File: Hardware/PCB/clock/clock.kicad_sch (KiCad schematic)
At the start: 62 parts, among them J1 AudioJack2, J2 Synth_power_2x5, J3 AudioJack2, J4 AudioJack2, J5 AudioJack2, J6 AudioJack2, J7 AudioJack2, J8 Conn_02x04_Odd_Even, J9 Conn_02x04_Odd_Even, SW1 RotaryEncoder, SW2 SW_Push, U1 40106

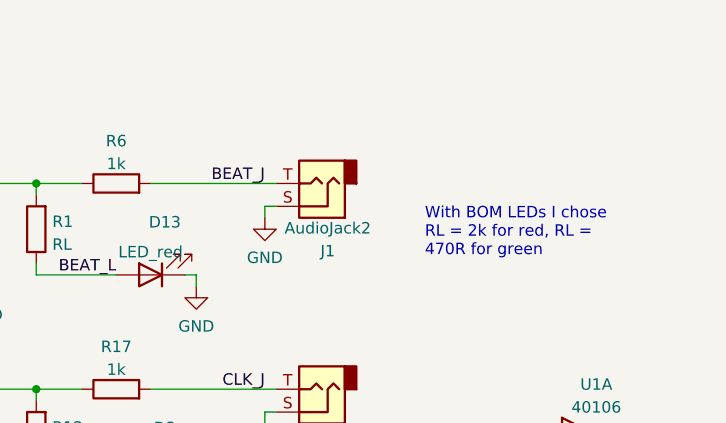
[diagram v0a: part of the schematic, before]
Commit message: LED notes on sch
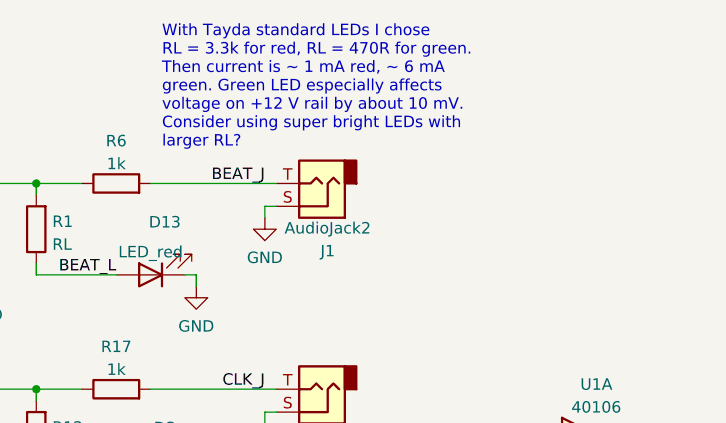
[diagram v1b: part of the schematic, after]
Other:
- note added: "With Tayda standard LEDs I chose RL = 3.3k for red, RL = 470R for green. Then current is ~ 1 mA red, ~ 6 mA green. Green LED especially affects voltage on +12 V rail by about 10 mV. Consider using super bright LEDs with larger RL?"
- note removed: "With BOM LEDs I chose RL = 2k for red, RL = 470R for green"
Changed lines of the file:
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@@
     )
   )
-  (text "With BOM LEDs I chose\nRL = 2k for red, RL = \n470R for green"
-    (at 233.68 40.005 0)
+  (text "With Tayda standard LEDs I chose\nRL = 3.3k for red, RL = 470R for green.\nThen current is ~ 1 mA red, ~ 6 mA\ngreen. Green LED especially affects\nvoltage on +12 V rail by about 10 mV.\nConsider using super bright LEDs with\nlarger RL?"
+    (at 204.47 27.94 0)
     (effects (font (size 1.27 1.27)) (justify left bottom))
   )

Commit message: PCB touch ups, panel
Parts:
- added GRAF3: AO logo, ao_tht:analogoutput_12mm, symbol ao_symbols:Graphic
- GRAF2: value Behind -> CC0 logo; footprint clock:clock_panel_holes -> ao_tht:CC0_logo
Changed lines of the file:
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@@
   (no_connect (at 260.35 77.47))
   (no_connect (at 157.48 60.96))
+  (polyline (pts (xy 13.97 13.97) (xy 13.97 160.02))
+    (stroke (width 0) (type default) (color 0 0 0 0))
+  )
   (wire (pts (xy 22.86 58.42) (xy 22.86 81.28))
     (stroke (width 0) (type default) (color 0 0 0 0))
@@
     (stroke (width 0) (type default) (color 0 0 0 0))
   )
+  (polyline (pts (xy 86.36 13.97) (xy 86.36 160.02))
+    (stroke (width 0) (type default) (color 0 0 0 0))
+  )
   (wire (pts (xy 139.7 78.74) (xy 142.24 78.74))
     (stroke (width 0) (type default) (color 0 0 0 0))
@@
     (stroke (width 0) (type default) (color 0 0 0 0))
   )
+  (polyline (pts (xy 13.97 13.97) (xy 86.36 13.97))
+    (stroke (width 0) (type default) (color 0 0 0 0))
+  )
   (wire (pts (xy 215.9 35.56) (xy 215.9 34.29))
     (stroke (width 0) (type default) (color 0 0 0 0))
@@
     (stroke (width 0) (type default) (color 0 0 0 0))
   )
+  (polyline (pts (xy 86.36 160.02) (xy 13.97 160.02))
+    (stroke (width 0) (type default) (color 0 0 0 0))
+  )
   (wire (pts (xy 24.13 104.14) (xy 17.78 104.14))
     (stroke (width 0) (type default) (color 0 0 0 0))
@@
     )
   )
-  (symbol (lib_id "ao_symbols:Graphic") (at 250.19 144.78 0) (unit 1)
-    (in_bom yes) (on_board yes)
-    (property "Reference" "GRAF2" (id 0) (at 257.2512 143.6116 0)
-      (effects (font (size 1.27 1.27)) (justify left))
-    )
-    (property "Value" "Behind" (id 1) (at 257.2512 145.923 0)
-      (effects (font (size 1.27 1.27)) (justify left))
-    )
-    (property "Footprint" "clock:clock_panel_holes" (id 2) (at 250.19 144.78 0)
-      (effects (font (size 1.27 1.27)) hide)
-    )
-    (property "Datasheet" "" (id 3) (at 250.19 144.78 0)
-      (effects (font (size 1.27 1.27)) hide)
-    )
-    (property "Config" "DNF" (id 4) (at 250.19 144.78 0)
-      (effects (font (size 1.27 1.27)) hide)
-    )
-  )
   (symbol (lib_id "ao_symbols:+5V_1") (at 50.8 96.52 0) (unit 1)
     (in_bom yes) (on_board yes) (fields_autoplaced)
@@
     (pin "2")
   )
+  (symbol (lib_id "ao_symbols:Graphic") (at 250.19 149.86 0) (unit 1)
+    (in_bom yes) (on_board yes)
+    (property "Reference" "GRAF3" (id 0) (at 257.2512 148.6916 0)
+      (effects (font (size 1.27 1.27)) (justify left))
+    )
+    (property "Value" "AO logo" (id 1) (at 257.2512 151.003 0)
+      (effects (font (size 1.27 1.27)) (justify left))
+    )
+    (property "Footprint" "ao_tht:analogoutput_12mm" (id 2) (at 250.19 149.86 0)
+      (effects (font (size 1.27 1.27)) hide)
+    )
+    (property "Datasheet" "" (id 3) (at 250.19 149.86 0)
+      (effects (font (size 1.27 1.27)) hide)
+    )
+    (property "Config" "DNF" (id 4) (at 250.19 149.86 0)
+      (effects (font (size 1.27 1.27)) hide)
+    )
+  )
   (symbol (lib_id "power:+5V") (at 144.145 22.86 0) (unit 1)
     (in_bom yes) (on_board yes) (fields_autoplaced)
@@
     (pin "2")
   )
+  (symbol (lib_id "ao_symbols:Graphic") (at 250.19 143.51 0) (unit 1)
+    (in_bom yes) (on_board yes)
+    (property "Reference" "GRAF2" (id 0) (at 257.2512 142.3416 0)
+      (effects (font (size 1.27 1.27)) (justify left))
+    )
+    (property "Value" "CC0 logo" (id 1) (at 257.2512 144.653 0)
+      (effects (font (size 1.27 1.27)) (justify left))
+    )
+    (property "Footprint" "ao_tht:CC0_logo" (id 2) (at 250.19 143.51 0)
+      (effects (font (size 1.27 1.27)) hide)
+    )
+    (property "Datasheet" "" (id 3) (at 250.19 143.51 0)
+      (effects (font (size 1.27 1.27)) hide)
+    )
+    (property "Config" "DNF" (id 4) (at 250.19 143.51 0)
+      (effects (font (size 1.27 1.27)) hide)
+    )
+  )
   (symbol (lib_id "ao_symbols:TestPoint") (at 104.14 199.39 0) (unit 1)
     (in_bom yes) (on_board yes) (fields_autoplaced)
@@
       (reference "GRAF1") (unit 1) (value "Holes") (footprint "clock:clock_panel_holes")
     )
-    (path "/3148a9e6-1e75-4e2a-b943-102cc5541cb8"
-      (reference "GRAF2") (unit 1) (value "Behind") (footprint "clock:clock_panel_holes")
+    (path "/dde30d9f-a4ed-4a0d-91aa-0eba4eadd958"
+      (reference "GRAF2") (unit 1) (value "CC0 logo") (footprint "ao_tht:CC0_logo")
+    )
+    (path "/419f3ecf-7b71-4a84-b495-f34f5fc91026"
+      (reference "GRAF3") (unit 1) (value "AO logo") (footprint "ao_tht:analogoutput_12mm")
     )
     (path "/9aa227a4-5918-4955-a2f5-b1e4c4fe38eb"

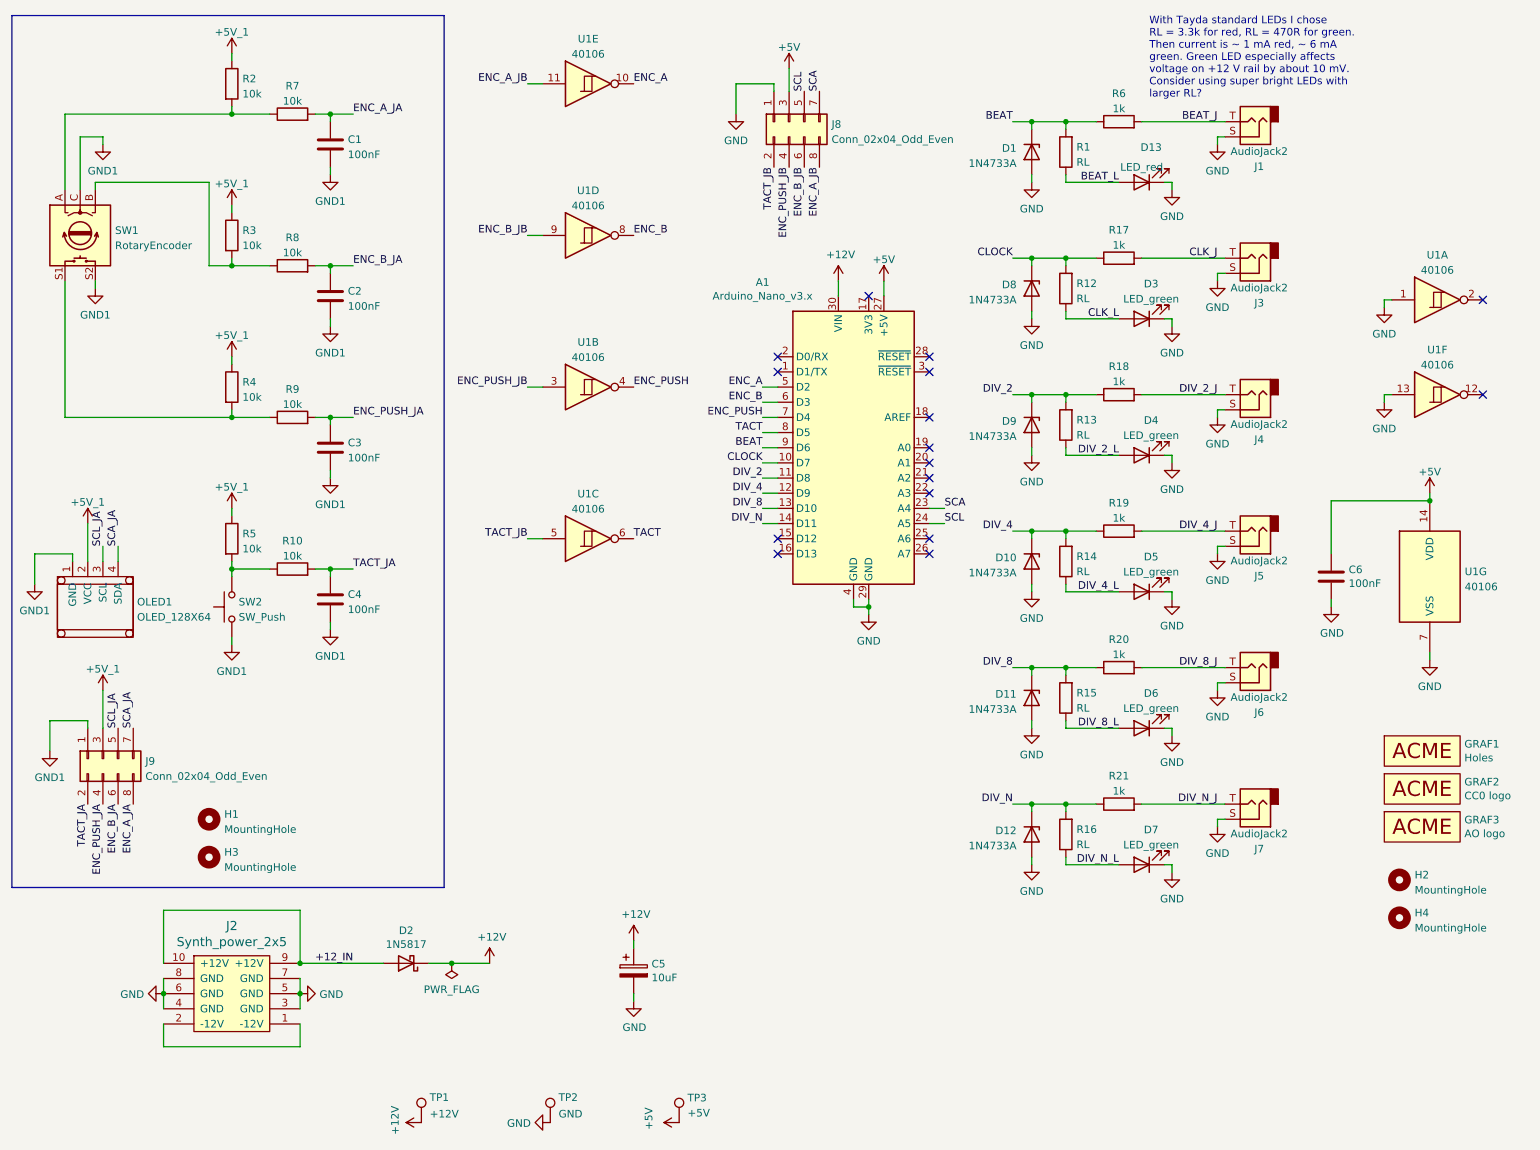
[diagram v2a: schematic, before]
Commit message: typo; OLED panel footprint
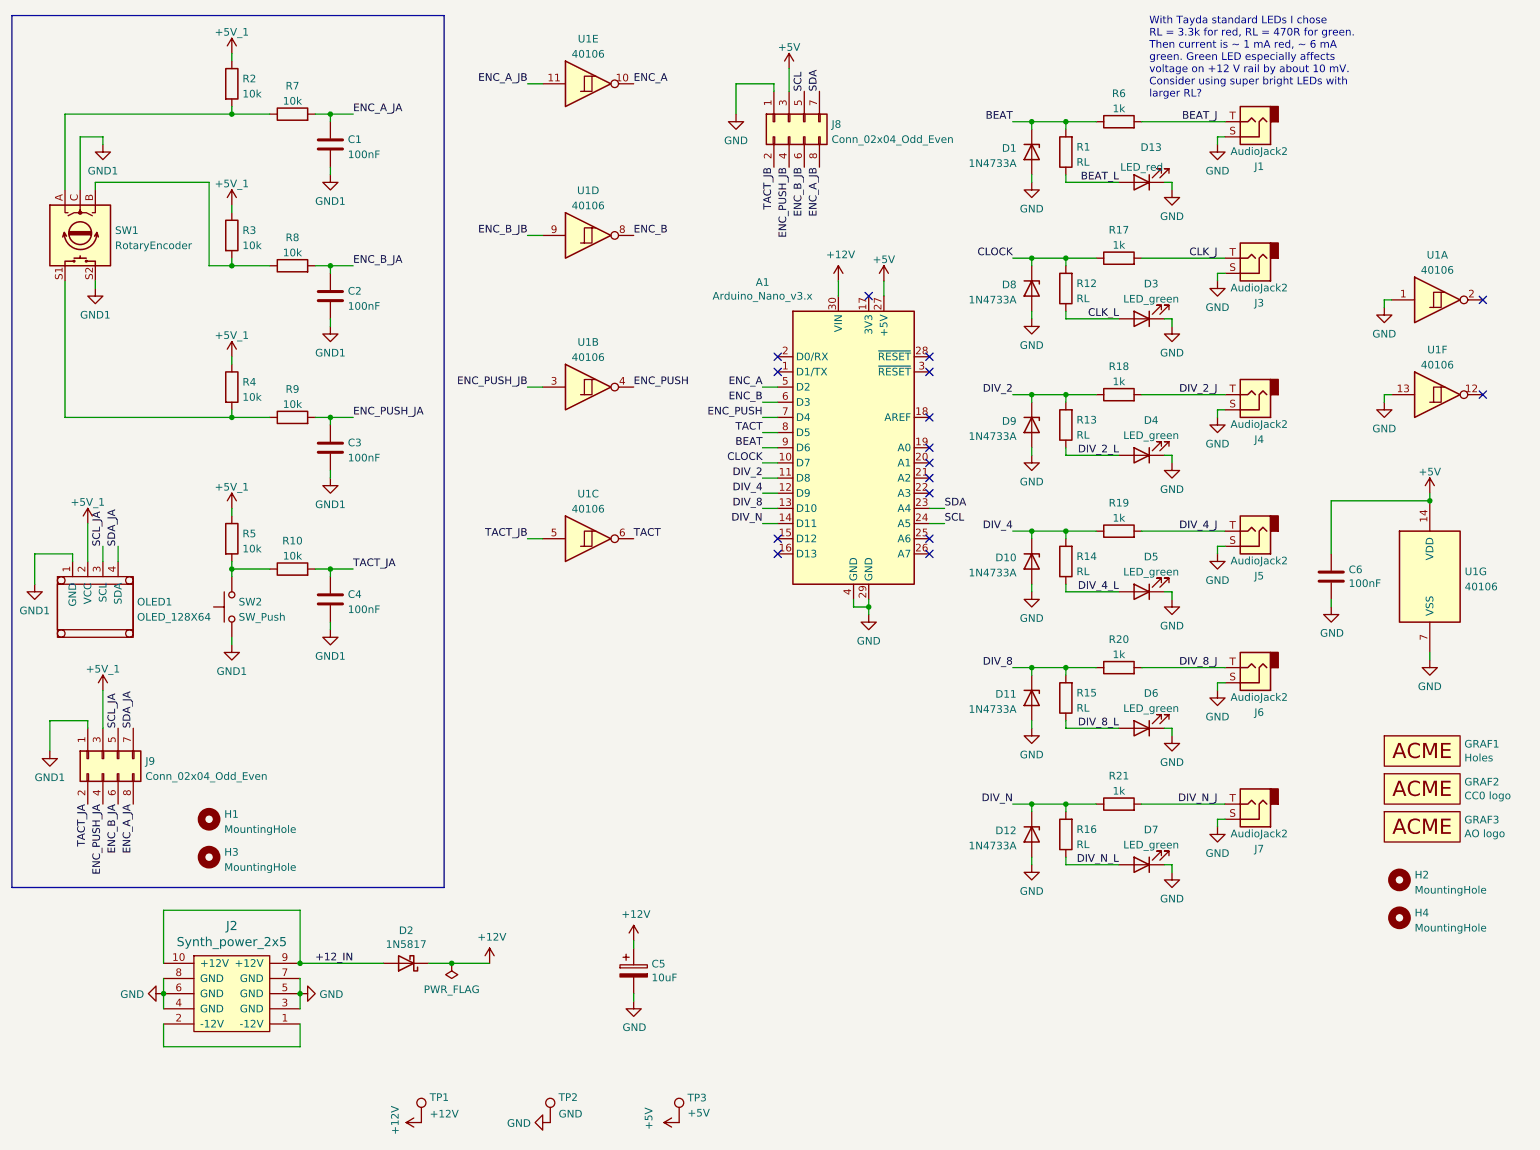
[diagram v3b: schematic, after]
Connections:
- net SCA renamed SDA
- net SCA_JA renamed SDA_JA
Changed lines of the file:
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@@
     (effects (font (size 1.27 1.27)) (justify right bottom))
   )
-  (label "SCA" (at 170.18 96.52 0)
+  (label "SDA" (at 170.18 96.52 0)
     (effects (font (size 1.27 1.27)) (justify left bottom))
   )
@@
     (effects (font (size 1.27 1.27)) (justify left bottom))
   )
-  (label "SCA_JA" (at 34.29 133.35 90)
+  (label "SDA_JA" (at 34.29 133.35 90)
     (effects (font (size 1.27 1.27)) (justify left bottom))
   )
@@
     (effects (font (size 1.27 1.27)) (justify right bottom))
   )
-  (label "SCA" (at 149.225 26.67 90)
+  (label "SDA" (at 149.225 26.67 90)
     (effects (font (size 1.27 1.27)) (justify left bottom))
   )
@@
     (effects (font (size 1.27 1.27)) (justify right bottom))
   )
-  (label "SCA_JA" (at 31.75 102.87 90)
+  (label "SDA_JA" (at 31.75 102.87 90)
     (effects (font (size 1.27 1.27)) (justify left bottom))
   )

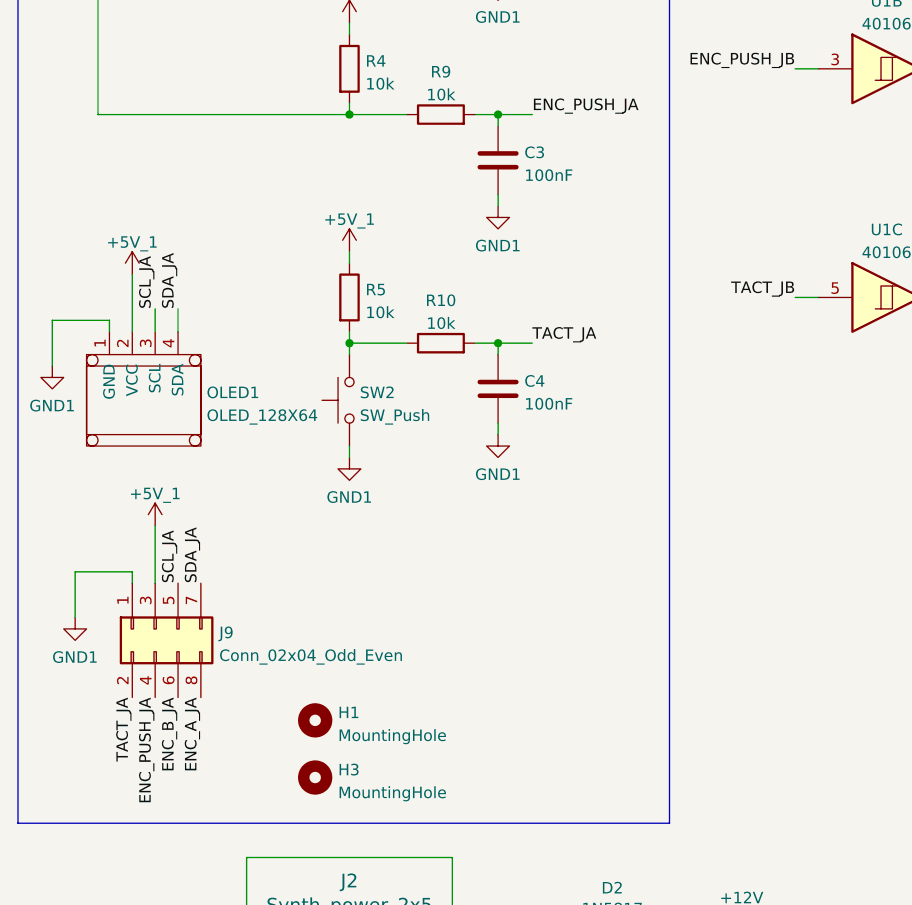
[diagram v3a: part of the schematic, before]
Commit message: Jumpers for OLED power
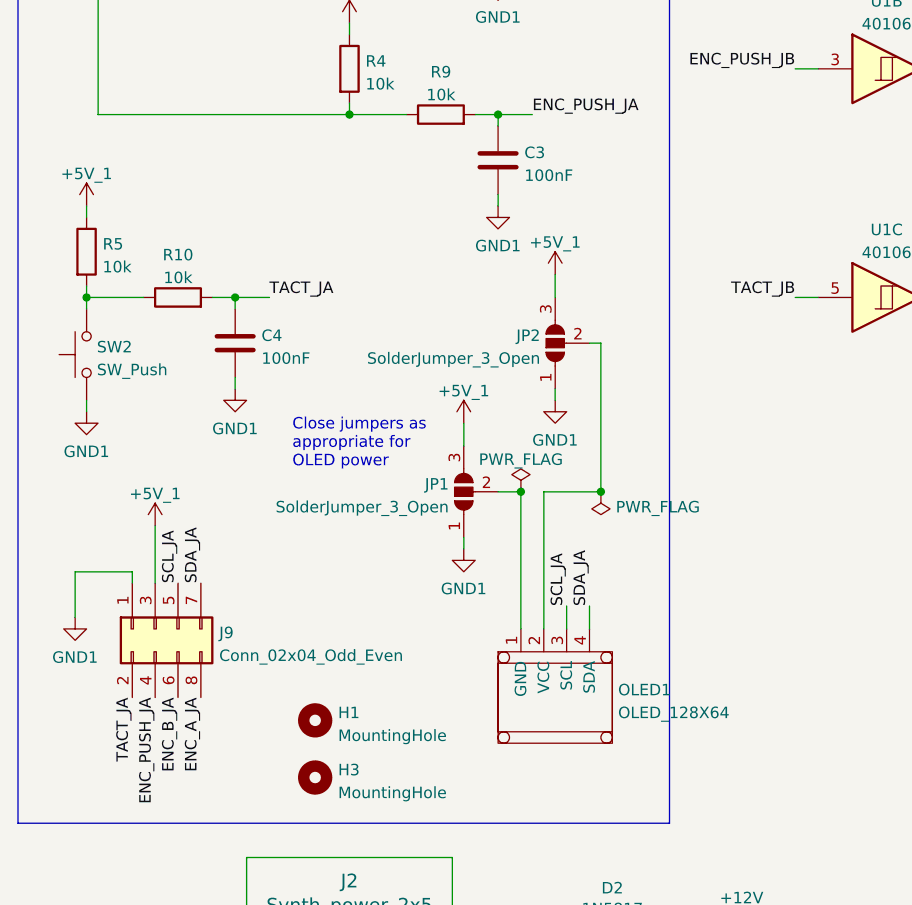
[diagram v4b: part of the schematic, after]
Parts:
- added JP1, JP2: SolderJumper_3_Open, Jumper:SolderJumper-3_P1.3mm_Open_RoundedPad1.0x1.5mm, symbol Jumper:SolderJumper_3_Open
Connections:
- net +5V_1: now also JP1.3 (B), JP2.3 (B); no longer OLED1.2 (VCC)
- net GND1: now also JP1.1 (A), JP2.1 (A); no longer OLED1.1 (GND)
- new net: JP1.2 (C), OLED1.1 (GND)
- new net: JP2.2 (C), OLED1.2 (VCC)
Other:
- note added: "Close jumpers as appropriate for OLED power"
- moved on the sheet: C4, OLED1, R10, R5, SW2
